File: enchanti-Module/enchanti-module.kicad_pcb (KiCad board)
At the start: 4 copper layers, 46 x 46 mm, 91 parts, among them J1 USB_C_Receptacle_USB2.0, J2 Programming Header, J3 Programming Header, SW2 KSC441G DCT 70SH LFS, U1 BQ25185DLHR, U10 ICM-42670-P, U11 IRIS-W106-30B, U12 MMC5633NJL, U2 STM32H7R3V8T6, U3 NCP167AMX180TBG, U4 B3U-1000P, U5 NCP167AMX330TBG, U6 USBLC6-2P6, U7 MAX17262REWL+T, U8 S76HS512TC0BHB010, U9 TCAN3413DRBR

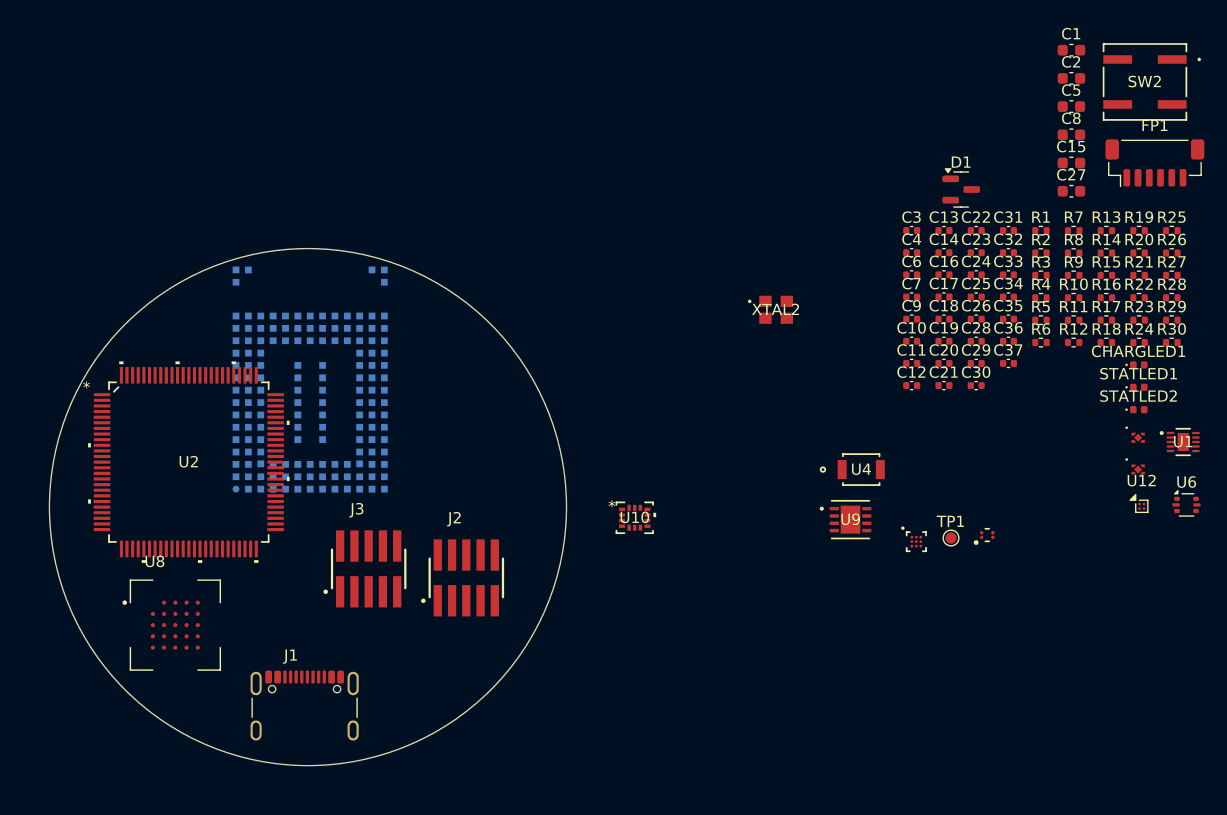
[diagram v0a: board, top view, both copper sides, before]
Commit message: added usb connector, added leds
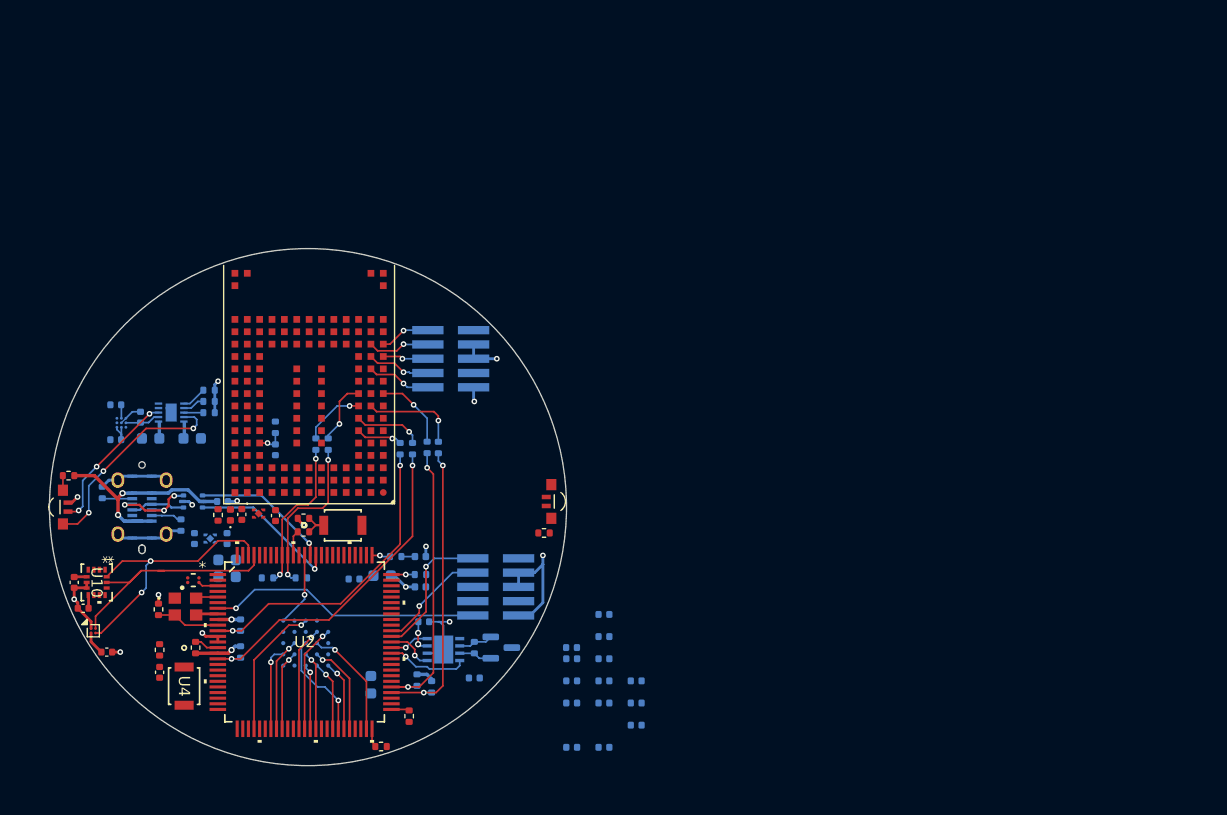
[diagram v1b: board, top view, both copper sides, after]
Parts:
- removed C31: 0.1uF, Capacitor_SMD:C_0402_1005Metric
- removed FP1: JST-SH-1x04 1.0mm, Connector_JST:JST_SH_BM06B-SRSS-TB_1x06-1MP_P1.00mm_Vertical
- removed J1: USB_C_Receptacle_USB2.0, Connector_USB:USB_C_Receptacle_GCT_USB4105-xx-A_16P_TopMnt_Horizontal
- removed SW2: KSC441G DCT 70SH LFS, ENCHANTI_switches:KSC-DCT_6P2X6P2_CNK
- removed TP1: CHRG TP, TestPoint:TestPoint_Pad_D1.0mm
- added D2: RGB-LED, ENCHANTI_leds:LED_APFA3010LSEEZGKQBKC, F.Cu at (114.4, 75.7)
- added D3: RGB-LED, ENCHANTI_leds:LED_APFA3010LSEEZGKQBKC, F.Cu at (70.9, 76.2)
- added R31: 1k, Resistor_SMD:R_0402_1005Metric, F.Cu at (71.4, 73.4)
- added U13: B3U-1000P, ENCHANTI_switches:B3U-1000P, F.Cu at (95.8, 77.8)
- added USB1: GSB1CA11101DSHR, ENCHANTI_connectors:AMPHENOL_GSB1CA11101DSHR, B.Cu at (77.9, 76.2)
- C1, C10, C11, C13, C14, C15, C16, C17, C18, C19, C2, C21, C22, C23, C24, C25, C26, C27, C28, C29, C3, C30, C33, C35, C36, C4, C5, C6, C8, C9, D1, J2, J3, R15, R16, R17, R18, R19, R2, R20, R21, R22, R23, R24, R25, R26, R27, R28, R29, R3, R30, R4, R6, R7, STATLED1, STATLED2, U1, U3, U6, U7, U8, U9: moved to B.Cu
- R10, R8: value 10k -> 1k
- U11: value IRIS-W106-30B -> IRIS-W106-00B; moved to F.Cu
- moved U12 93.9 mm to (73.6, 87.2)
- moved U1 90.1 mm to (80.5, 67.8)
- moved R7 89.5 mm to (74.4, 74.9), turned to -90 degrees
- moved U6 88.4 mm to (82.5, 75.7)
- moved R19 88.3 mm to (86.7, 89.1), turned to -90 degrees
- moved C32 88.2 mm to (72.7, 85.2), turned to 180 degrees
- moved C5 87.1 mm to (78.7, 70.1), turned to 180 degrees
- moved R9 86.7 mm to (79.4, 85.3), turned to 90 degrees
- moved R20 86.5 mm to (86.7, 86.7), turned to -90 degrees
- moved C34 86.2 mm to (74.8, 89.1)
- moved C1 85.5 mm to (82.4, 70.1)
- moved C37 85.4 mm to (71.9, 82.9), turned to -90 degrees
- moved C8 84.1 mm to (85.5, 80.9), turned to 180 degrees
- moved R1 83.9 mm to (82.7, 88.7), turned to 90 degrees
- moved R5 83.7 mm to (79.5, 88.9), turned to -90 degrees
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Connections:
- net /INT_LED1 renamed /INT_LEDB
- net /INT_LED2 renamed /INT_LEDO
- D1 pad 1: /CAN_L -> /CAN_H
- D1 pad 2: /CAN_H -> /CAN_L
- J2 pad 6: /JTDO -> unconnected-(J2-SWO-Pad6)
- J2 pad 8: /JTDI -> unconnected-(J2-TDI-Pad8)
- J3 pad 10: /RES -> /JTAG_nRST
- J3 pad 2: /SWDA -> /JTAG_TMS
- J3 pad 4: /SWCLK -> /JTAG_TCK
- J3 pad 6: unconnected-(J3-SWO-Pad6) -> /JTAG_TDO
- J3 pad 8: unconnected-(J3-TDI-Pad8) -> /JTAG_TDI
- R10 pad 1: +1V8 -> +3V3
- R10 pad 2: /RSTO# -> Net-(D2-Pad2)
- R14 pad 1: /BOOT -> GND
- R8 pad 1: +1V8 -> /BOOT
- R8 pad 2: Net-(U8-RESET#) -> Net-(R14-Pad2)
- U1 pad 4: /CE -> GND
- U11 pad A12: unconnected-(U11A-JTAG_TDO-PadA12) -> /JTAG_TDO
- U11 pad A14: unconnected-(U11A-JTAG_TMS-PadA14) -> /JTAG_TMS
- U11 pad B11: unconnected-(U11A-JTAG_nRST-PadB11) -> /JTAG_nRST
- U11 pad B12: unconnected-(U11A-JTAG_TDI-PadB12) -> /JTAG_TDI
- U11 pad B14: unconnected-(U11A-JTAG_TCK-PadB14) -> /JTAG_TCK
- U2 pad 100: unconnected-(U2A-PB9-Pad100) -> /BTN2
- U2 pad 18: /BTN1 -> unconnected-(U2A-PA2-Pad18)
- U2 pad 19: /BTN2 -> /I2S6_MCK
- U2 pad 2: unconnected-(U2A-PC13-Pad2) -> /LED1
- U2 pad 21: /LED1 -> /I2S6_WS/SPI1_NSS
- U2 pad 22: /LED2 -> /I2S6_CK/SPI1_SCK
- U2 pad 24: unconnected-(U2A-PA6-Pad24) -> /I2S6_SDI/SPI1_MISO
- U2 pad 25: unconnected-(U2A-PA7-Pad25) -> /I2S6_SDO/SPI1_MOSI
- U2 pad 26: unconnected-(U2A-PB0-Pad26) -> /ANG1
- U2 pad 27: unconnected-(U2A-PB1-Pad27) -> /ANG2
- U2 pad 28: unconnected-(U2A-PB2-Pad28) -> /ANG3
- U2 pad 60: unconnected-(U2A-PA9-Pad60) -> /LED2
- U2 pad 61: unconnected-(U2A-PA10-Pad61) -> /CAN_MODE
- U2 pad 66: /JTDI -> unconnected-(U2A-PA15-Pad66)
- U2 pad 73: /EN_3V3REG -> unconnected-(U2A-PM0-Pad73)
- U2 pad 74: /CAN_MODE -> /EN_3V3REG
- U2 pad 89: /RSTO# -> unconnected-(U2A-PM13-Pad89)
- U2 pad 93: unconnected-(U2A-PB5-Pad93) -> /LED2
- U2 pad 99: unconnected-(U2A-PB8-Pad99) -> /BTN1
- U8 pad A2: /RSTO# -> unconnected-(U8-RSTO#-PadA2)
- U8 pad A4: Net-(U8-RESET#) -> unconnected-(U8-RESET#-PadA4)
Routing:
- net GND: track 0.00 -> 57.6 mm, vias 0 -> 15
- net /SDMMC_CMD: track 0.00 -> 30.0 mm, vias 0 -> 2
- net /SDMMC_CLK: track 0.00 -> 29.2 mm, vias 0 -> 2
- net /SDMMC_D0: track 0.00 -> 26.4 mm, vias 0 -> 2
- net /SDMMC_D1: track 0.00 -> 26.3 mm, vias 0 -> 2
- net /NRST: track 0.00 -> 24.3 mm, vias 0 -> 1
- net /I3C_SDA: track 0.00 -> 23.7 mm, vias 0 -> 2
- net /I3C_SCL: track 0.00 -> 22.0 mm
- net VUSB: track 0.00 -> 21.4 mm, vias 0 -> 2
- net /STAT1: track 0.00 -> 18.7 mm, vias 0 -> 3
- net /SDMMC_D2: track 0.00 -> 14.7 mm, vias 0 -> 2
- net /SDMMC_D3: track 0.00 -> 13.7 mm, vias 0 -> 2
- net /USBD-: track 0.00 -> 13.5 mm, vias 0 -> 1
- net /STAT2: track 0.00 -> 13.0 mm, vias 0 -> 3
- net /SWDIO: track 0.00 -> 12.5 mm, vias 0 -> 1
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
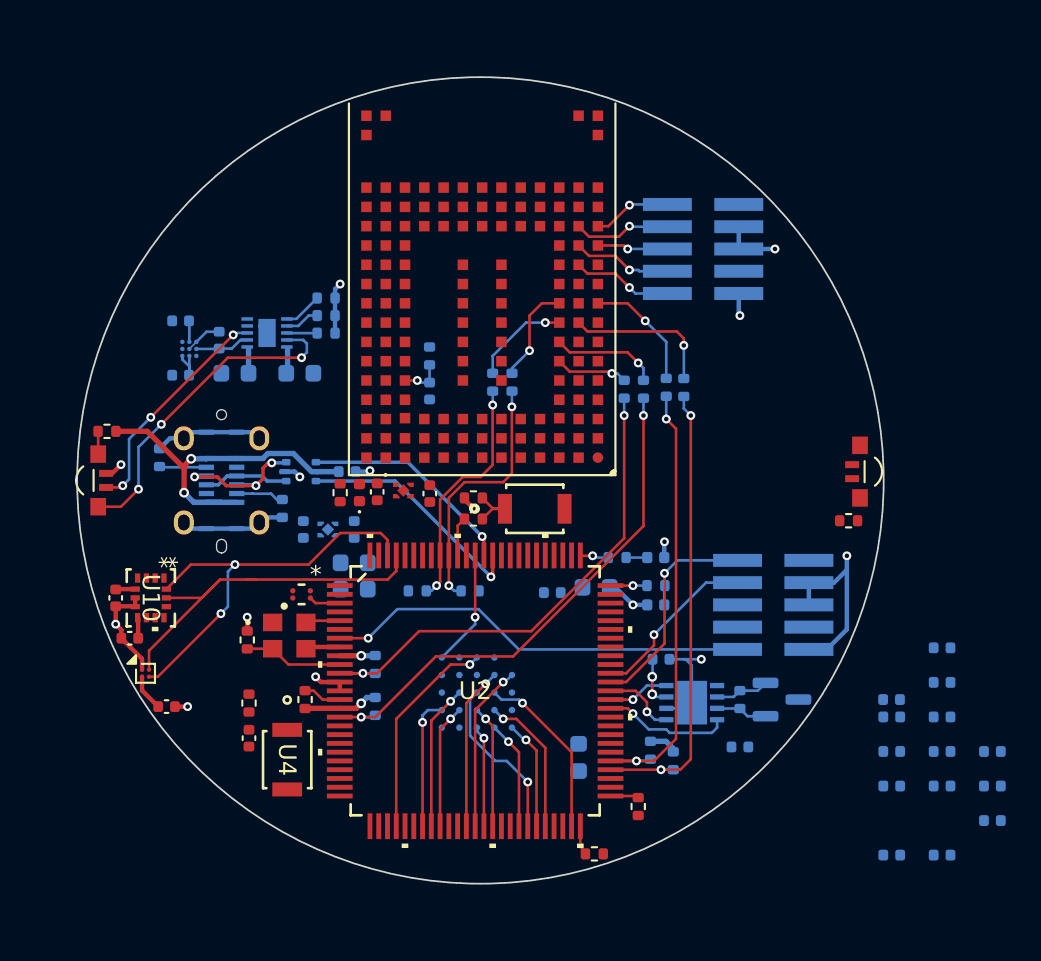
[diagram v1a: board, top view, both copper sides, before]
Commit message: added battery module, initial routing for power and data traces
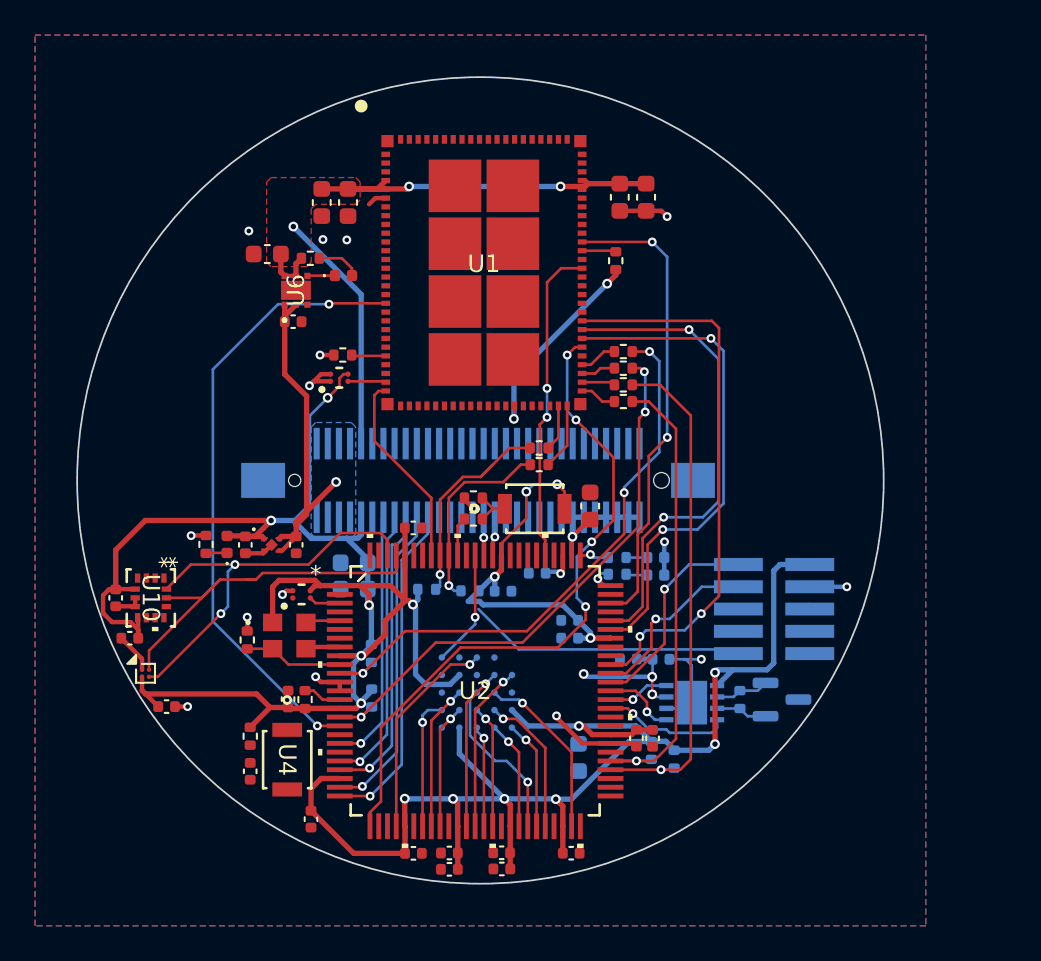
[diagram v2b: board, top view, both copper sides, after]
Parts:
- removed C23: 0.1uF, Capacitor_SMD:C_0402_1005Metric
- removed C24: 0.47uF, Capacitor_SMD:C_0402_1005Metric
- removed C33: 1uF, Capacitor_SMD:C_0402_1005Metric
- removed CHARGLED1: S1, LED_SMD:LED_0402_1005Metric
- removed D2, D3: RGB-LED, ENCHANTI_leds:LED_APFA3010LSEEZGKQBKC
- removed J3: Programming Header, ENCHANTI_connectors:SAMTEC_FTSH-105-01-F-DV-P-TR
- removed R24: 47k, Resistor_SMD:R_0402_1005Metric
- removed R26, R27, R28, R29, R30: 30, Resistor_SMD:R_0402_1005Metric
- removed R31: 1k, Resistor_SMD:R_0402_1005Metric
- removed U11: IRIS-W106-00B, ENCHANTI_WiFi:IRIS-W106
- removed U5: NCP167AMX330TBG, ENCHANTI_regulators:XDFN4_1X1_711AJ_ONS
- removed U7: MAX17262REWL+T, ENCHANTI_battery-management:MAX17262
- removed USB1: GSB1CA11101DSHR, ENCHANTI_connectors:AMPHENOL_GSB1CA11101DSHR
- added J5: CONN_MEZANNINE, ENCHANTI_connectors:CON_536250674_MOL, B.Cu at (92.6, 76.2)
- added PGLED1: PGLED1, LED_SMD:LED_0402_1005Metric, F.Cu at (84.9, 64.5)
- added PGLED2: S1, LED_SMD:LED_0402_1005Metric, F.Cu at (78.3, 79.8)
- added XTAL3: SIT1552AC-JE-DCC-32.768E, ENCHANTI_crystal-resonators:BGA4_SiT1532_SIT, F.Cu at (84.7, 70.3)
- C1, C10, C11, C17, C18, C21, C22, C25, C26, C27, C28, C30, C4, C5, C6, C9, R25, U3: moved to F.Cu
- C13: value 0.1uF -> 10uF; footprint Capacitor_SMD:C_0402_1005Metric -> Capacitor_SMD:C_0603_1608Metric; moved to F.Cu
- C20: value 1uF -> 10uF; footprint Capacitor_SMD:C_0402_1005Metric -> Capacitor_SMD:C_0603_1608Metric
- C3: value 1uF -> 10uF; footprint Capacitor_SMD:C_0402_1005Metric -> Capacitor_SMD:C_0603_1608Metric; moved to F.Cu
- R11: value 1k -> 10k
- R12, R13: value 2k2 -> 30
- R2: value 13k -> 10k; moved to F.Cu
- R21, R22, R23: value 47k -> 10k
- R3: value 0.43k -> 10k; moved to F.Cu
- R4: value 10k -> 30; moved to F.Cu
- R6, R7: value 5k1 -> 30; moved to F.Cu
- U1: value BQ25185DLHR -> Sona-IF573; footprint ENCHANTI_battery-management:WSON10_DLH_TEX -> ENCHANTI_WiFi:Sona-IF573; moved to F.Cu
- U6: value USBLC6-2P6 -> NCP187AMT330TAG; footprint Package_TO_SOT_SMD:SOT-666 -> ENCHANTI_regulators:NCV8187AMT330TAG_ONS; moved to F.Cu
- moved C9 40.3 mm to (81.7, 88.7), turned to 90 degrees
- moved R10 36.7 mm to (77.1, 79.8), turned to 90 degrees
- moved C10 36.2 mm to (88.9, 78.9), turned to 0 degrees
- moved C28 33.2 mm to (83.0, 95.5), turned to -90 degrees
- moved C18 30.7 mm to (88.9, 97.5), turned to 0 degrees
- moved C11 28.1 mm to (93.9, 98.4)
- moved C19 27.4 mm to (94.0, 82.5), turned to 0 degrees
- moved C17 26.3 mm to (93.9, 97.4)
- moved C26 25.9 mm to (90.9, 97.5)
- moved R13 25.9 mm to (100.9, 71.7)
- moved C3 25.7 mm to (102.2, 60.0), turned to -90 degrees
- moved C30 25.2 mm to (90.9, 98.4)
- moved R7 21.7 mm to (96.1, 74.3), turned to 180 degrees
- moved C16 21.5 mm to (97.8, 84.2)
- moved R6 21.4 mm to (100.9, 68.8), turned to 0 degrees
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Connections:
- C1 pad 1: VUSB -> +3V3
- C13 pad 1: +BATT -> +3V3
- C3 pad 1: CHRG+ -> +3V3
- C5 pad 1: SYS -> +3V3
- R10 pad 1: +3V3 -> Net-(PGLED2-K)
- R10 pad 2: Net-(D2-Pad2) -> GND
- R11 pad 1: Net-(CHARGLED1-K) -> +3V3
- R11 pad 2: GND -> Net-(PGLED1-A)
- R12 pad 1: /I2C2_SDA -> /SDIO_DATA2
- R12 pad 2: +1V8 -> /SDMMC_D2
- R13 pad 1: /I2C2_SCL -> /SDIO_DATA1
- R13 pad 2: +1V8 -> /SDMMC_D1
- R17 pad 1: +3V3 -> +1V8
- R17 pad 2: /PDn -> /SDMMC_D3
- R2 pad 1: GND -> /BT_INTERFACE_SELECT
- R2 pad 2: /VSET -> +1V8
- R21 pad 2: /SDMMC_D3 -> /SDMMC_D2
- R22 pad 2: /SDMMC_D2 -> /SDMMC_D1
- R23 pad 2: /SDMMC_D1 -> /SDMMC_D0
- R25 pad 1: /SDIO_CMD -> /SDIO_DATA0
- R25 pad 2: /SDMMC_CMD -> /SDMMC_D0
- R3 pad 1: GND -> /SDIO_SELECT
- R3 pad 2: /ISET -> GND
- R4 pad 1: GND -> /SDIO_CMD
- R4 pad 2: /TMR -> /SDMMC_CMD
- R6 pad 1: GND -> /SDIO_CLK
- R6 pad 2: Net-(USB1-CC2) -> /SDMMC_CLK
- R7 pad 1: GND -> /SDIO_DATA3
- R7 pad 2: Net-(USB1-CC1) -> /SDMMC_D3
- U1 pad 1: SYS -> unconnected-(U1-UC-Pad1)
- U1 pad 10: VUSB -> unconnected-(U1-UC-Pad10)
- U1 pad 11: GND -> unconnected-(U1-GPIO_3_WL_JTAG_TM-Pad11)
- U1 pad 2: CHRG+ -> unconnected-(U1-UC-Pad2)
- U1 pad 3: /STAT2 -> unconnected-(U1-UC-Pad3)
- U1 pad 4: GND -> +3V3
- U1 pad 5: GND -> +3V3
- U1 pad 6: /TMR -> GND
- U1 pad 7: /VSET -> unconnected-(U1-UC-Pad7)
- U1 pad 8: /ISET -> unconnected-(U1-UC-Pad8)
- U1 pad 9: /STAT1 -> unconnected-(U1-UC-Pad9)
- U2 pad 17: unconnected-(U2A-PA1-Pad17) -> /WL_DEV_WAKE
- U2 pad 26: /ANG1 -> /BT_UART4_CTS
- U2 pad 66: unconnected-(U2A-PA15-Pad66) -> /BT_UART4_RTS
- U2 pad 70: unconnected-(U2A-PC10-Pad70) -> /BT_UART4_TX
- U2 pad 71: unconnected-(U2A-PC11-Pad71) -> /BT_UART4_RX
- U2 pad 73: unconnected-(U2A-PM0-Pad73) -> /BT_DEV_WAKE
- U2 pad 74: /EN_3V3REG -> unconnected-(U2A-PM1-Pad74)
- U2 pad 80: unconnected-(U2A-PM5-Pad80) -> /BT_REG_ON
- U2 pad 93: /LED2 -> /WL_REG_ON
- U6 pad 1: /D- -> SYS
- U6 pad 2: GND -> SYS
- U6 pad 3: /D+ -> GND
- U6 pad 4: /USBD+ -> Net-(PGLED1-K)
- U6 pad 5: VUSB -> +3V3
- U6 pad 6: /USBD- -> +3V3
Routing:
- net +1V8: track 12.3 -> 214.5 mm, vias 2 -> 19
- net +3V3: track 2.87 -> 80.2 mm, vias 2 -> 6
- net /BT_UART4_CTS: track 0.00 -> 38.4 mm, vias 0 -> 4
- net /WL_DEV_WAKE: track 0.00 -> 35.5 mm, vias 0 -> 2
- net /BT_UART4_RTS: track 0.00 -> 31.5 mm, vias 0 -> 2
- net /BT_UART4_TX: track 0.00 -> 28.6 mm, vias 0 -> 2
- net /BT_UART4_RX: track 0.00 -> 27.9 mm, vias 0 -> 2
- net /BT_DEV_WAKE: track 0.00 -> 26.8 mm, vias 0 -> 2
- net SYS: track 1.42 -> 21.0 mm, vias 0 -> 1
- net GND: track 57.6 -> 38.4 mm, vias 15 -> 16
- net /I2S6_SDO/SPI1_MOSI: track 0.00 -> 19.0 mm, vias 0 -> 1
- net /STAT1: track 18.7 -> 0.00 mm, vias 3 -> 0
- net /BT_REG_ON: track 0.00 -> 18.2 mm, vias 0 -> 2
- net /I2S6_SDI/SPI1_MISO: track 0.00 -> 18.0 mm, vias 0 -> 1
- net /I2S6_CK/SPI1_SCK: track 0.00 -> 17.1 mm, vias 0 -> 1
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- added copper zone on F.Cu, net +3V3
- added copper zone on B.Cu, net GND
- added copper zone on F.Cu, net GND
- added copper zone on In1.Cu, net GND
- added copper zone on In2.Cu, net GND
- added copper zone on B.Cu, net SYS
